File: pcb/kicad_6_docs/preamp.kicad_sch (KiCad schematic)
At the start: 47 parts, among them J1 pre_in_pcb, J2 ts_pcb, J3 gain_pcb, J4 pre_out_pcb, J5 pre_hv_dc_in_pcb, J6 pre_dc_htr_in_pcb

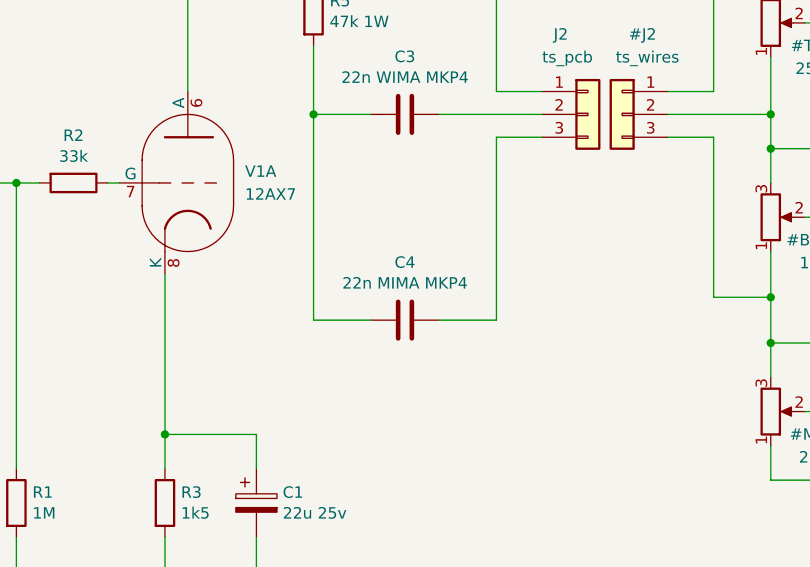
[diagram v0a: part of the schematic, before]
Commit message: fix capacitor name typo
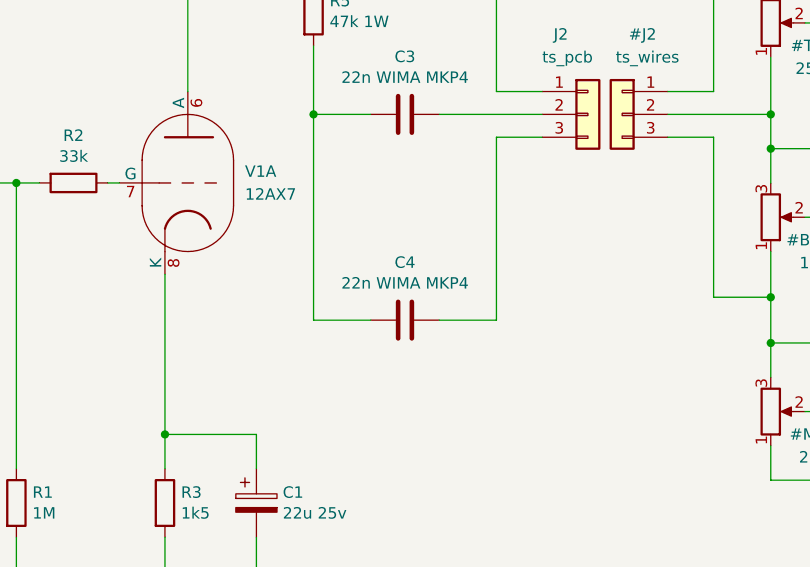
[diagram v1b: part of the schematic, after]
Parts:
- C4: value 22n MIMA MKP4 -> 22n WIMA MKP4
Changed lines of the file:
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@@
     (in_bom yes) (on_board yes)
     (property "Reference" "C4" (id 0) (at 97.79 107.8992 90))
-    (property "Value" "22n MIMA MKP4" (id 1) (at 97.79 110.2106 90))
+    (property "Value" "22n WIMA MKP4" (id 1) (at 97.79 110.2106 90))
     (property "Footprint" "Capacitor_THT:C_Rect_L13.0mm_W4.0mm_P10.00mm_FKS3_FKP3_MKS4" (id 2) (at 93.98 115.2652 0)
       (effects (font (size 1.27 1.27)) hide)

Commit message: tweak some values
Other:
- note added: "265VDC"
- note added: "bleeder"
- note removed: "270VDC"
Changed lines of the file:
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@@
+    (stroke (width 0) (type default) (color 0 0 0 0))
+  )
+  (wire (pts (xy 207.01 196.85) (xy 209.55 196.85))
     (stroke (width 0) (type default) (color 0 0 0 0))
   )
@@
   )
   (wire (pts (xy 299.72 85.09) (xy 297.18 85.09))
+    (stroke (width 0) (type default) (color 0 0 0 0))
+  )
+  (wire (pts (xy 207.01 194.31) (xy 209.55 194.31))
     (stroke (width 0) (type default) (color 0 0 0 0))
   )
@@
     (effects (font (size 2.9972 2.9972)) (justify left bottom))
   )
+  (text "bleeder" (at 179.07 52.07 0)
+    (effects (font (size 1.27 1.27)) (justify left bottom))
+  )
   (text "Heaters are configured\nfor 12.6 volt operation." (at 177.8 185.42 0)
     (effects (font (size 2.9972 2.9972)) (justify left bottom))
@@
     (effects (font (size 1.27 1.27)) (justify left bottom))
   )
-  (text "270VDC" (at 223.52 25.4 0)
+  (text "265VDC" (at 224.79 25.4 0)
     (effects (font (size 1.27 1.27)) (justify left bottom))
   )
@@
     (effects (font (size 1.27 1.27)) (justify left))
   )
-  (hierarchical_label "pre_dc_htr_in_2" (shape input) (at 207.01 196.85 0)
+  (hierarchical_label "pre_dc_htr_in_2" (shape input) (at 209.55 196.85 0)
     (effects (font (size 1.27 1.27)) (justify left))
   )
@@
     (effects (font (size 1.27 1.27)) (justify left))
   )
-  (hierarchical_label "pre_dc_htr_in_1" (shape input) (at 207.01 194.31 0)
-    (effects (font (size 1.27 1.27)) (justify left))
-  )
+  (hierarchical_label "pre_dc_htr_in_1" (shape input) (at 209.55 194.31 0)
+    (effects (font (size 1.27 1.27)) (justify left))
+  )
